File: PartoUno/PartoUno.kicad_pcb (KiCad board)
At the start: 2 copper layers, 80 x 99.2 mm, 71 parts, among them J10 RED5, J11 GRE3, J12 GRE2, J13 RED4, J14 GNC_BOND, J15 GNC_BOND, J16 GNC_BOND, J17 GNC_BOND, J18 GNC_BOND, J19 GNC_BOND, J2 WHI3, J20 GNC_BOND, J21 GNC_BOND, J22 GNC_BOND, J23 GNC_BOND, J24 GNC_BOND, J25 GNC_BOND, J26 GNC_BOND, J27 GNC_BOND, J28 GNC_BOND, J29 GNC_BOND, J3 YEL5, J30 GNC_BOND, J31 GNC_BOND, J32 GNC_BOND, J33 GNC_BOND, J34 GNC_BOND, J35 GNC_BOND, J4 BLU1, J5 BLU2, J6 YEL4, J7 WHI4, J8 YEL3, J9 GRE1, U1 ATtiny45V-10S, U2 74HC595, U3 74HC595, U4 74HC595

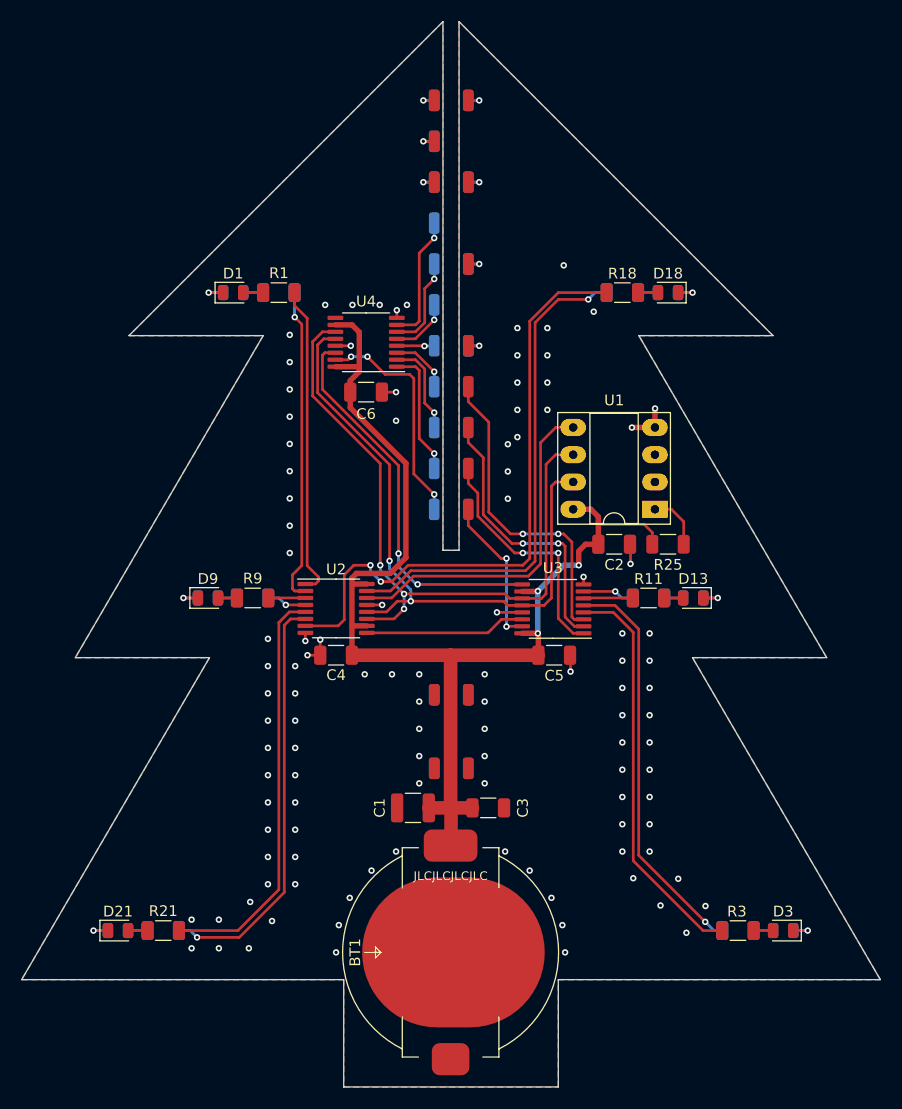
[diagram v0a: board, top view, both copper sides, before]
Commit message: Fixed code
Had an issue in shiftOutData where I defined the wrong data type (16 bit instead of 32 bit) so it cut all data short
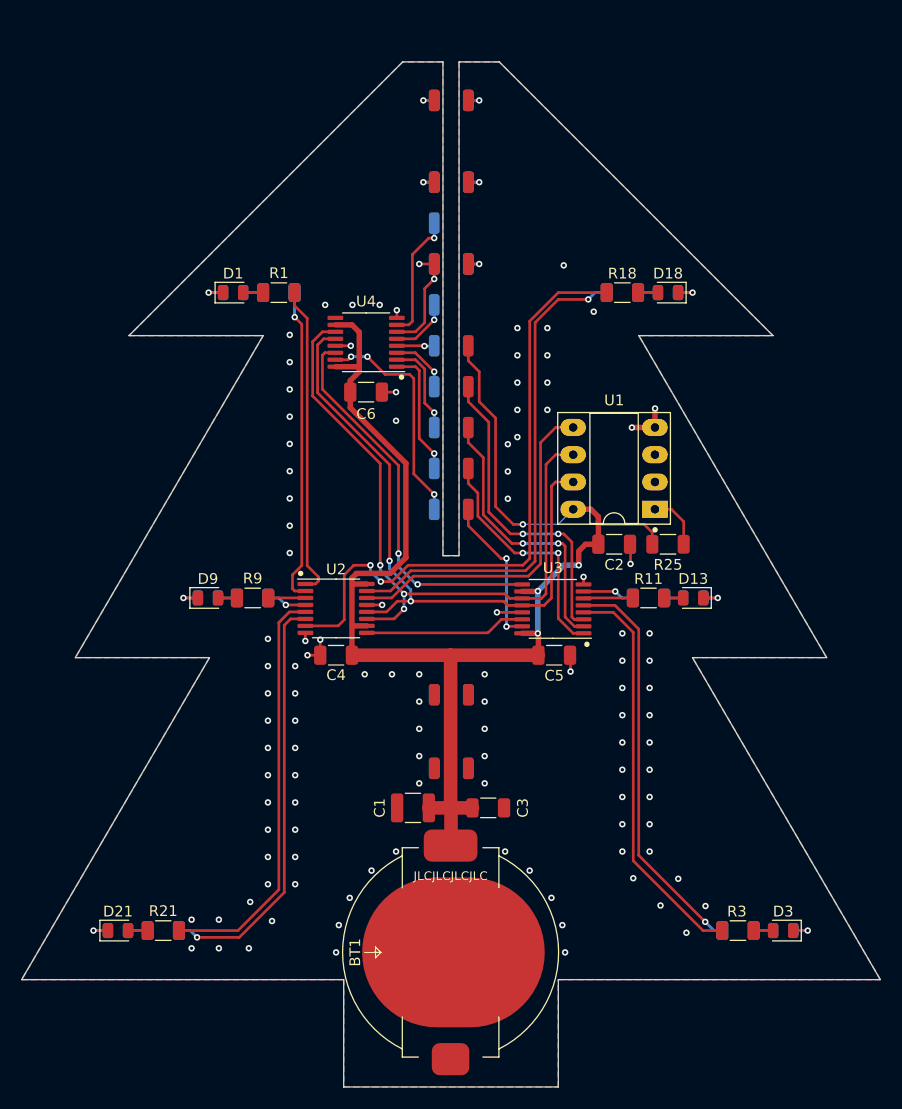
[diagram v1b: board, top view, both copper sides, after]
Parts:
- removed J15, J22, J27: GNC_BOND, Connector_Wire:SolderWirePad_1x01_SMD_1x2mm
- added J1: GNC_BOND, Connector_Wire:SolderWirePad_1x01_SMD_1x2mm, F.Cu at (138.9, 76.3)
- J17: value GNC_BOND -> GND_BOND
- J20: value GNC_BOND -> TOP_STAR_VCC
- moved S1 6.00 mm to (135.0, 147.7)
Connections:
- J20 pad 1: GND -> VCC
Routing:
- net VCC: track 111.4 -> 135.9 mm, vias 3 -> 4
- net GND: track 52.2 -> 49.5 mm, vias 125 -> 123
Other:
- board size 80 x 99.2 mm -> 80 x 95.5 mm
